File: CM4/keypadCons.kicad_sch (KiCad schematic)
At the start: 13 parts, among them J4 USB_A, J5 USB_A, U7 TUSB4041I, Y1 24 MHz

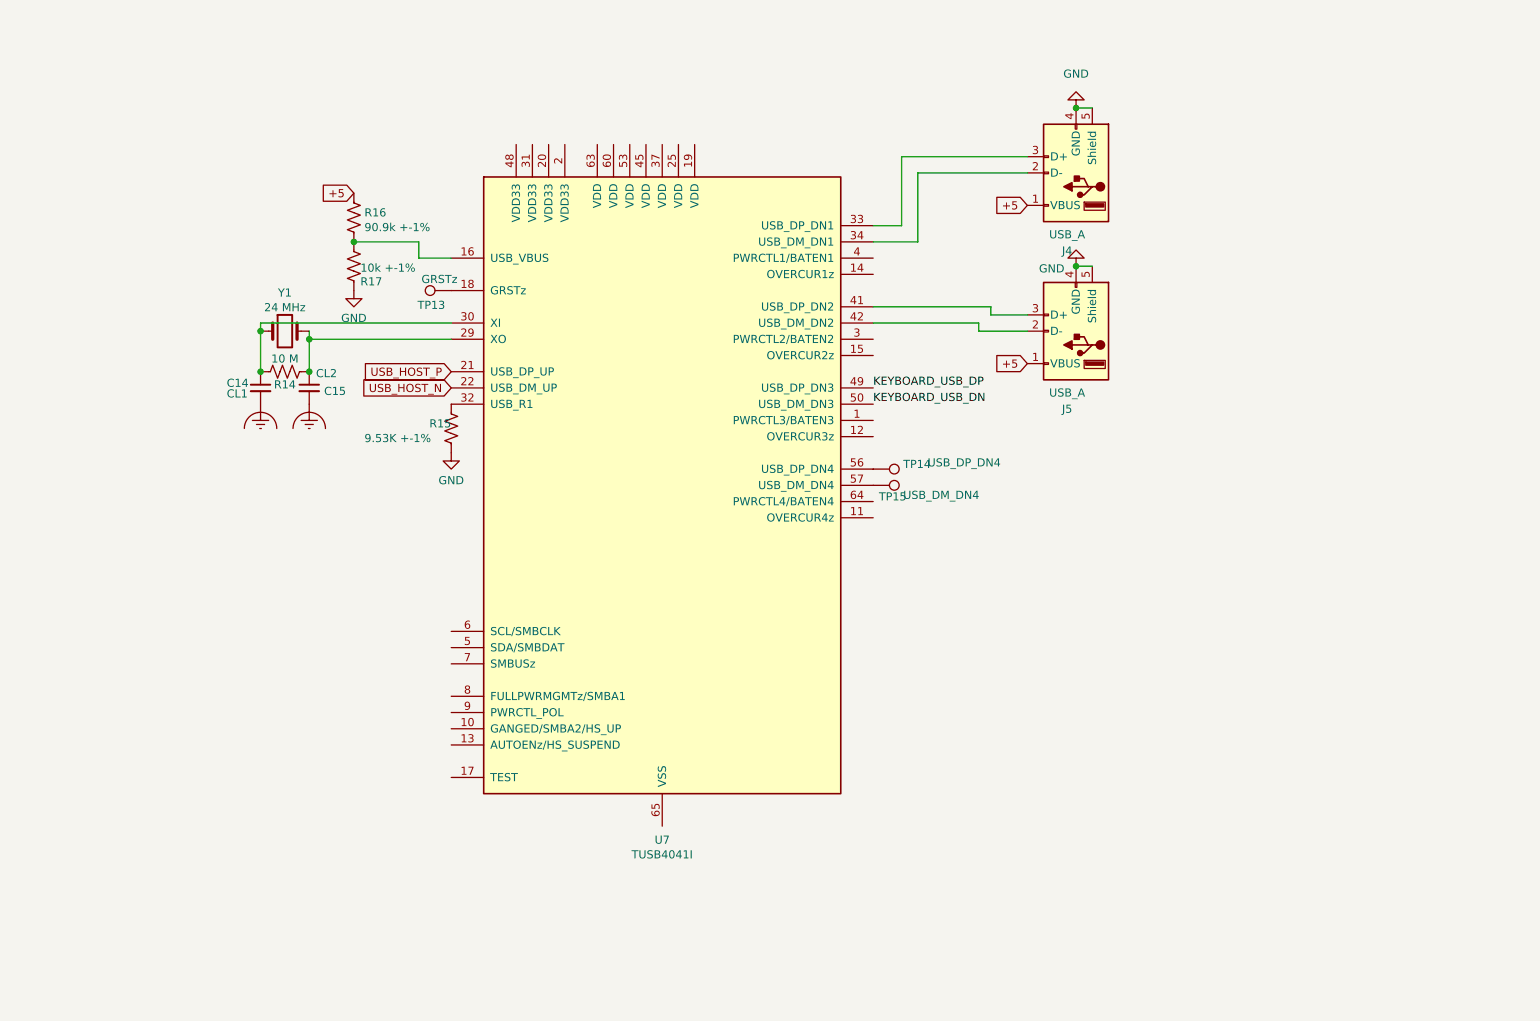
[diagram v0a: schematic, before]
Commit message: Added Keyboard matrix controller and indicator leds
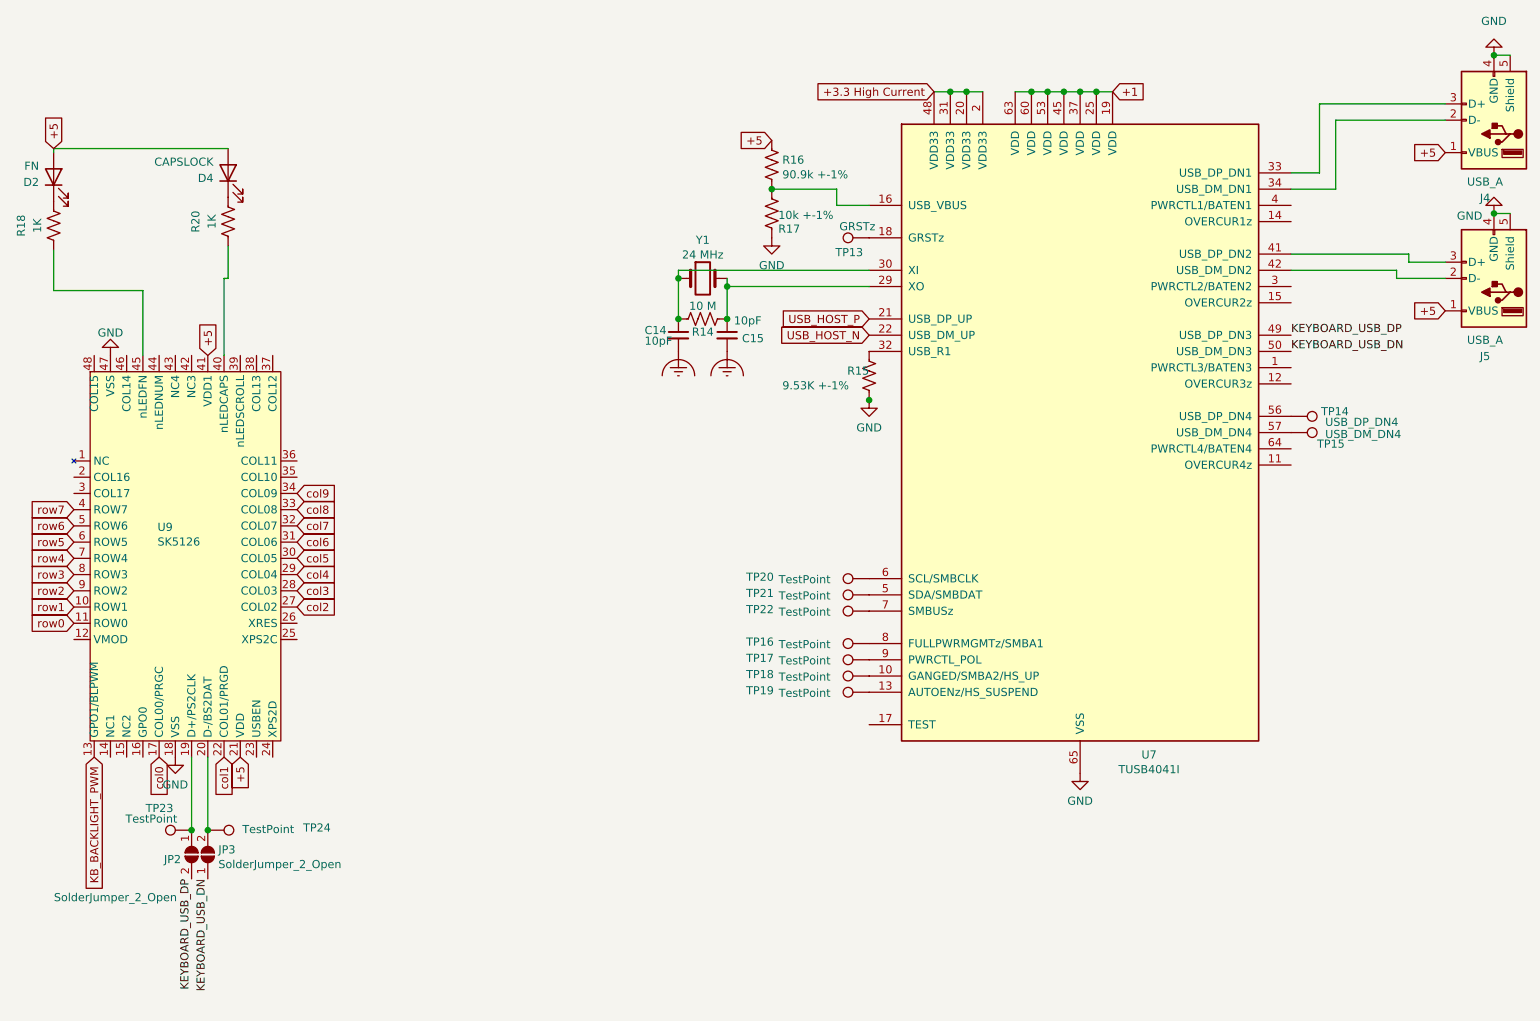
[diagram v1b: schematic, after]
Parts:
- added D2: FN, LED_SMD:LED_1206_3216Metric_Pad1.42x1.75mm_HandSolder, symbol Device:LED
- added D4: CAPSLOCK, LED_SMD:LED_1206_3216Metric_Pad1.42x1.75mm_HandSolder, symbol Device:LED
- added JP2, JP3: SolderJumper_2_Open, Jumper:SolderJumper-2_P1.3mm_Open_RoundedPad1.0x1.5mm, symbol Jumper:SolderJumper_2_Open
- added R18, R20: 1K, Resistor_SMD:R_1206_3216Metric, symbol Device:R_US
- added TP16, TP17, TP18, TP19, TP20, TP21, TP22, TP23, TP24: TestPoint, TestPoint:TestPoint_Pad_1.0x1.0mm, symbol Connector:TestPoint
- added U9: SK5126, Package_DFN_QFN:QFN-48-1EP_7x7mm_P0.5mm_EP5.6x5.6mm, symbol teensy:SK5126
- C14: value CL1 -> 10pF
- C15: value CL2 -> 10pF
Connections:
- net +5: now also D2.2 (A), D4.2 (A), U9.21 (VDD), U9.41 (VDD1)
- net GND: now also U7.65 (VSS), U9.18 (VSS), U9.47 (VSS)
- net KEYBOARD_USB_DN: now also JP3.1 (A)
- net KEYBOARD_USB_DP: now also JP2.2 (B)
- net at U7.10 (GANGED/SMBA2/HS_UP): now also TP18.1
- net at U7.13 (AUTOENz/HS_SUSPEND): now also TP19.1
- net +1: now reaches U7.19 (VDD)
- net +1: now also U7.25 (VDD), U7.37 (VDD), U7.45 (VDD), U7.53 (VDD), U7.60 (VDD), U7.63 (VDD)
- net +3.3 High Current: now reaches U7.2 (VDD33)
- net +3.3 High Current: now also U7.20 (VDD33), U7.31 (VDD33), U7.48 (VDD33)
- net at U7.5 (SDA/SMBDAT): now also TP21.1
- net at U7.6 (SCL/SMBCLK): now also TP20.1
- net at U7.7 (SMBUSz): now also TP22.1
- net at U7.8 (FULLPWRMGMTz/SMBA1): now also TP16.1
- net at U7.9 (PWRCTL_POL): now also TP17.1
- new net: R18.1, U9.45 (nLEDFN)
- new net: D2.1 (K), R18.2
- new net: JP2.1 (A), TP23.1, U9.19 (D+/PS2CLK)
- new net: R20.1, U9.40 (nLEDCAPS)
- new net: D4.1 (K), R20.2
- new net: JP3.2 (B), TP24.1, U9.20 (D-/BS2DAT)
- new net KB_BACKLIGHT_PWM: U9.13 (GPO1/BLPWM)
- new net col0: U9.17 (COL00/PRGC)
- new net col1: U9.22 (COL01/PRGD)
- new net col2: U9.27 (COL02)
- new net col3: U9.28 (COL03)
- new net col4: U9.29 (COL04)
- new net col5: U9.30 (COL05)
- new net col6: U9.31 (COL06)
- new net col7: U9.32 (COL07)
- new net col8: U9.33 (COL08)
- new net col9: U9.34 (COL09)
- new net row0: U9.11 (ROW0)
- new net row1: U9.10 (ROW1)
- new net row2: U9.9 (ROW2)
- new net row3: U9.8 (ROW3)
- new net row4: U9.7 (ROW4)
- new net row5: U9.6 (ROW5)
- new net row6: U9.5 (ROW6)
- new net row7: U9.4 (ROW7)
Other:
- moved on the sheet: C14, C15, J4, J5, R14, R15, R16, R17, TP13, TP14, TP15, U7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

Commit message: Cleaned Up the Matrix contolller
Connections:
- net GND: now also U9.49 (GND)
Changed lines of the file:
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@@
+    (pin "1")
+  )
+  (symbol (lib_id "power:GND") (at 88.265 118.11 0) (unit 1)
+    (in_bom yes) (on_board yes)
+    (property "Reference" "#PWR0146" (id 0) (at 88.265 124.46 0)
+      (effects (font (size 1.27 1.27)) hide)
+    )
+    (property "Value" "GND" (id 1) (at 88.265 122.4344 0))
+    (property "Footprint" "" (id 2) (at 88.265 118.11 0)
+      (effects (font (size 1.27 1.27)) hide)
+    )
+    (property "Datasheet" "" (id 3) (at 88.265 118.11 0)
+      (effects (font (size 1.27 1.27)) hide)
+    )
     (pin "1")
   )
@@
     (pin "47")
     (pin "48")
+    (pin "49")
     (pin "5")
     (pin "6")
